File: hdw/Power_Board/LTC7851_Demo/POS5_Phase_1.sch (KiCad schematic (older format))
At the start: 37 parts, among them U301 LTC7851UHH, U401 SiC779

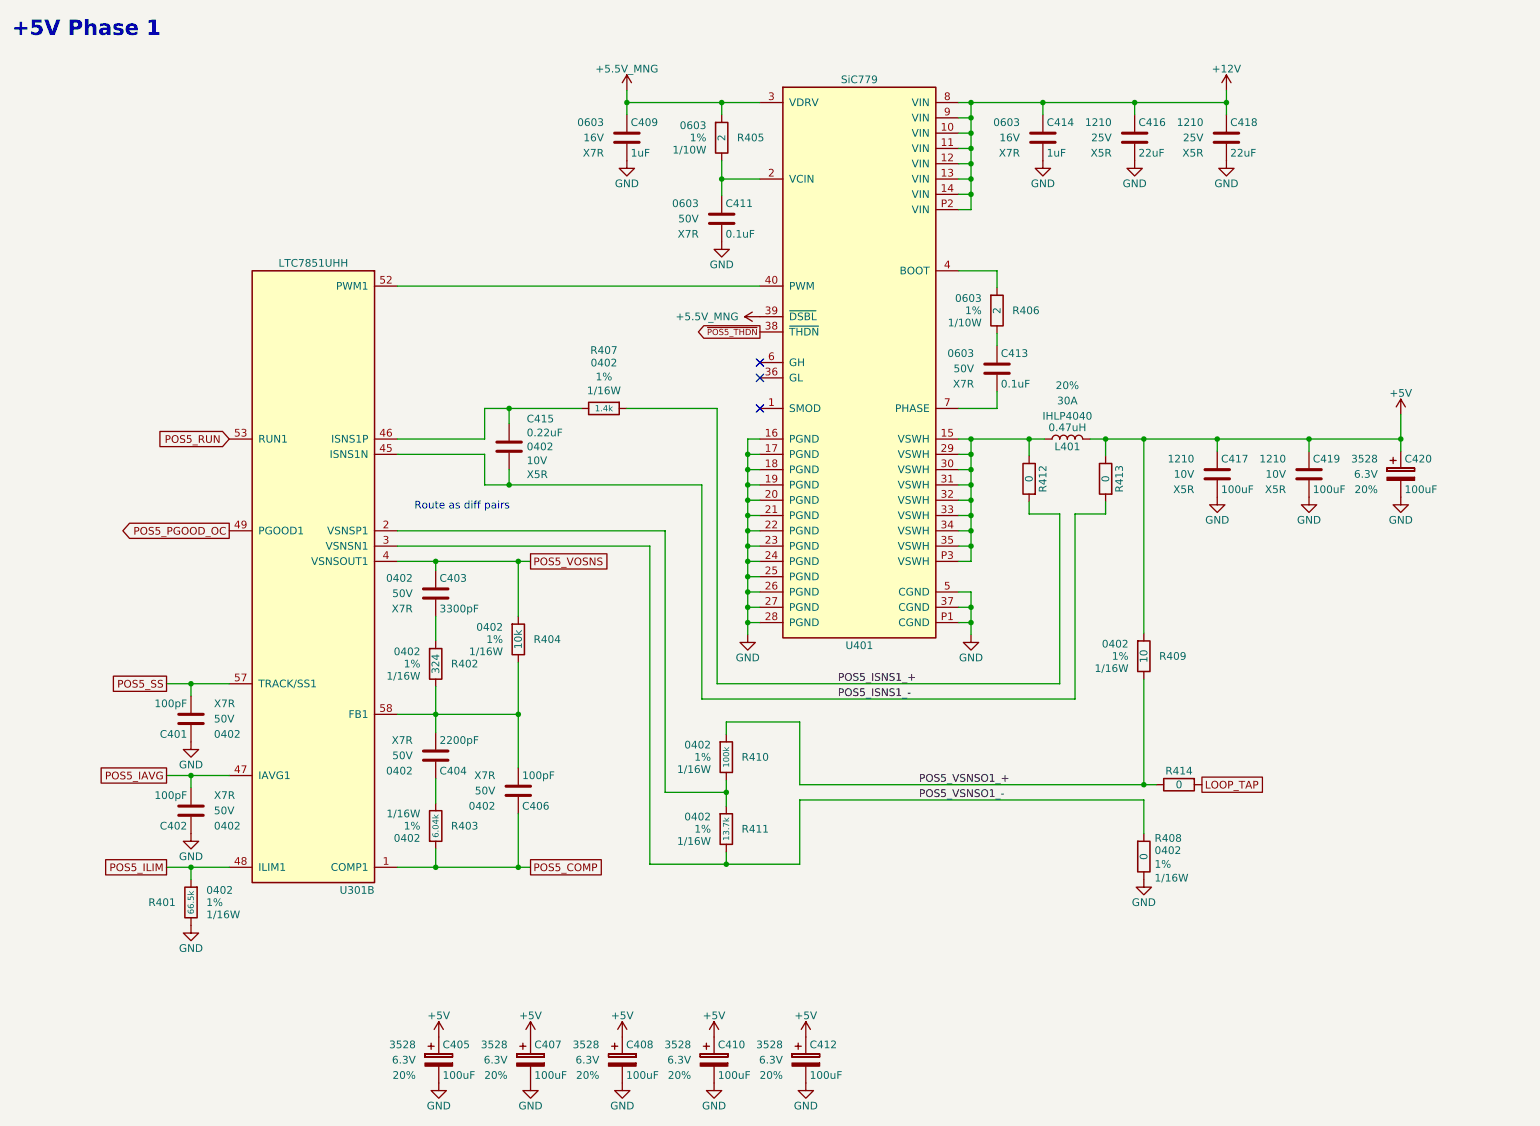
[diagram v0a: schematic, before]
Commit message: Added changes to power board BOM
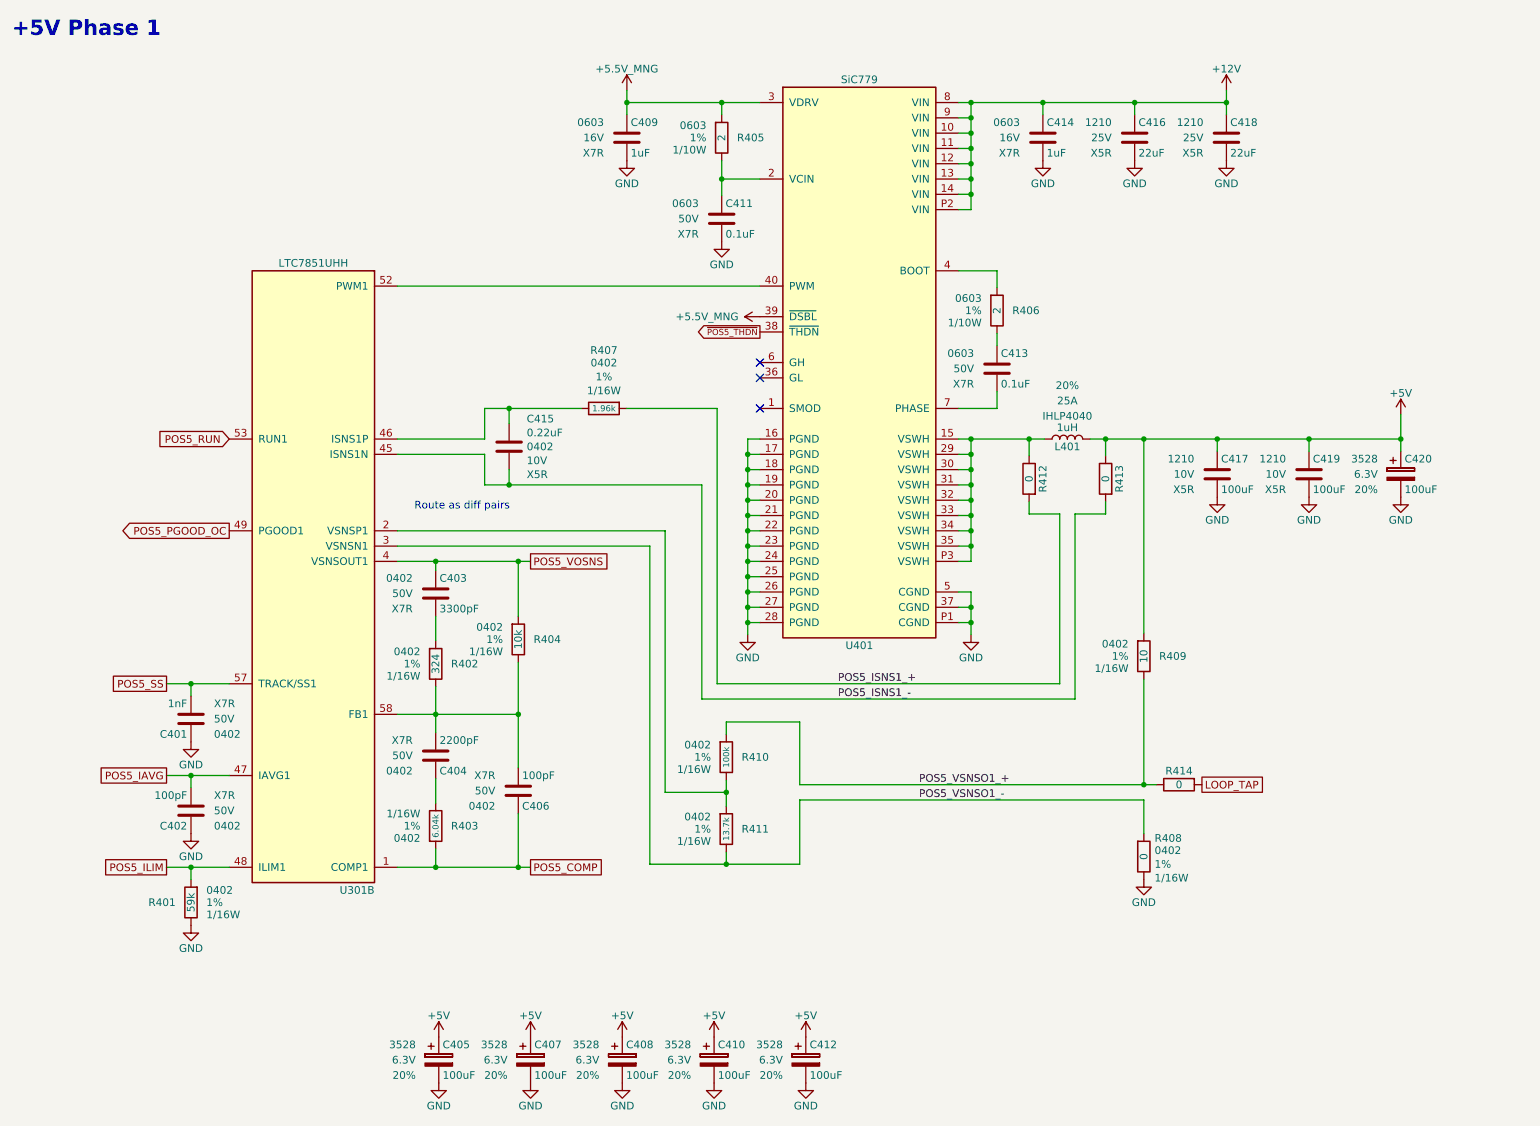
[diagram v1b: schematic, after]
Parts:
- C401: value 100pF -> 1nF; Digi-Key PN 478-1089-1-ND -> 311-1080-1-ND
- L401: value 0.47uH -> 1uH; Ampacity 30A -> 25A; Digi-Key PN 541-2595-1-ND -> 541-1306-1-ND
- R401: value 66.5k -> 59k; Digi-Key PN RMCF0402FT66K5CT-ND -> P59KDCCT-ND
- R407: value 1.4k -> 1.96k; Digi-Key PN RMCF0402FT1K40CT-ND -> 311-1.96KLRCT-ND
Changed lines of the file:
@@
 P 7440 3310
 F 0 "L401" V 7390 3310 50  0000 C CNN
-F 1 "0.47uH" V 7515 3310 50  0000 C CNN
+F 1 "1uH" V 7515 3310 50  0000 C CNN
 F 2 "Inductors_SMD:L_Vishay_IHLP-4040" H 7440 3310 50  0001 C CNN
 F 3 "" H 7440 3310 50  0001 C CNN
-F 4 "541-2595-1-ND" H 7440 3310 50  0001 C CNN "Digi-Key PN"
+F 4 "541-1306-1-ND" H 7440 3310 50  0001 C CNN "Digi-Key PN"
 F 5 "IHLP4040" V 7590 3310 50  0000 C CNN "display_footprint"
-F 6 "30A" V 7690 3310 50  0000 C CNN "Ampacity"
+F 6 "25A" V 7690 3310 50  0000 C CNN "Ampacity"
 F 7 "20%" V 7790 3310 50  0000 C CNN "Tolerance"
 	1    7440 3310
@@
 P 4410 3110
 F 0 "R407" V 4790 3110 50  0000 C CNN
-F 1 "1.4k" V 4410 3110 40  0000 C CNN
+F 1 "1.96k" V 4410 3110 40  0000 C CNN
 F 2 "Resistors_SMD:R_0402" H 4410 3110 50  0001 C CNN
 F 3 "" H 4410 3110 50  0001 C CNN
-F 4 "RMCF0402FT1K40CT-ND" H 4710 3510 60  0001 C CNN "Digi-Key PN"
+F 4 "311-1.96KLRCT-ND" H 4710 3510 60  0001 C CNN "Digi-Key PN"
 F 5 "0402" V 4708 3110 50  0000 C CNN "display_footprint"
 F 6 "1%" V 4617 3110 50  0000 C CNN "Tolerance"
@@
 P 1710 6340
 F 0 "R401" H 1610 6340 50  0000 R CNN
-F 1 "66.5k" V 1710 6340 40  0000 C CNN
+F 1 "59k" V 1710 6340 50  0000 C CNN
 F 2 "Resistors_SMD:R_0402" H 1710 6340 50  0001 C CNN
 F 3 "" H 1710 6340 50  0001 C CNN
-F 4 "RMCF0402FT66K5CT-ND" H 2010 6740 60  0001 C CNN "Digi-Key PN"
+F 4 "P59KDCCT-ND" H 2010 6740 60  0001 C CNN "Digi-Key PN"
 F 5 "0402" H 1810 6420 50  0000 L CNN "display_footprint"
 F 6 "1%" H 1810 6340 50  0000 L CNN "Tolerance"
@@
 P 1710 5140
 F 0 "C401" H 1735 5240 50  0000 L CNN
-F 1 "100pF" H 1735 5040 50  0000 L CNN
+F 1 "1nF" H 1735 5040 50  0000 L CNN
 F 2 "Capacitors_SMD:C_0402" H 1748 4990 50  0001 C CNN
 F 3 "" H 1735 5240 50  0001 C CNN
-F 4 "478-1089-1-ND" H 2135 5640 60  0001 C CNN "Digi-Key PN"
+F 4 "311-1080-1-ND" H 2135 5640 60  0001 C CNN "Digi-Key PN"
 F 5 "0402" H 1560 5240 50  0000 R CNN "display_footprint"
 F 6 "50V" H 1560 5140 50  0000 R CNN "Voltage"

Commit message: Merging drews_branch_3 into master
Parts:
- C401, C402, C403, C404, C406, C409, C411, C413, C414, C415, C416, C417, C418, C419: symbol Custom_Library:C_Custom -> LED_Display_Local_Library:C_Custom
- C405, C407, C408, C410, C412, C420: symbol Custom_Library:CP_Tant_Custom -> LED_Display_Local_Library:CP_Tant_Custom
- L401: symbol Custom_Library:L_Custom -> LED_Display_Local_Library:L_Custom
- R401, R402, R403, R404, R405, R406, R407, R408, R409, R410, R411, R412, R413, R414: symbol Custom_Library:R_Custom -> LED_Display_Local_Library:R_Custom
- U301: symbol Custom_Library:LTC7851UHH -> LED_Display_Local_Library:LTC7851UHH
- U401: symbol Custom_Library:SiC779 -> LED_Display_Local_Library:SiC779
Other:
- note added: "04. +5V Phase 1"
- note removed: "+5V Phase 1"
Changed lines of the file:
@@
 POS5_PGOOD_OC
 $Comp
-L Custom_Library:C_Custom C409
+L LED_Display_Local_Library:C_Custom C409
 U 1 1 5BB875B8
 P 4560 1340
@@
 F 2 "Capacitors_SMD:C_0603" H 4598 1190 50  0001 C CNN
 F 3 "" H 4585 1440 50  0001 C CNN
-F 4 "0603" H 4410 1440 50  0000 R CNN "display_footprint"
-F 5 "16V" H 4410 1340 50  0000 R CNN "Voltage"
-F 6 "X7R" H 4410 1240 50  0000 R CNN "Dielectric"
-F 7 "1276-6524-1-ND" H 4985 1840 60  0001 C CNN "Digi-Key PN"
+F 4 "1276-6524-1-ND" H 4985 1840 60  0001 C CNN "Digi-Key PN"
+F 5 "0603" H 4410 1440 50  0000 R CNN "display_footprint"
+F 6 "16V" H 4410 1340 50  0000 R CNN "Voltage"
+F 7 "X7R" H 4410 1240 50  0000 R CNN "Dielectric"
 	1    4560 1340
 	1    0    0    -1
@@
 $EndComp
 $Comp
-L Custom_Library:SiC779 U401
+L LED_Display_Local_Library:SiC779 U401
 U 1 1 5BB8C7AD
 P 6080 2810
@@
 	6810 3910 6810 4010
 $Comp
-L Custom_Library:L_Custom L401
+L LED_Display_Local_Library:L_Custom L401
 U 1 1 5BB98C10
 P 7440 3310
@@
 	6810 1710 6810 1810
 $Comp
-L Custom_Library:R_Custom R406
+L LED_Display_Local_Library:R_Custom R406
 U 1 1 5BB9AE0E
 P 6980 2470
@@
 $EndComp
 $Comp
-L Custom_Library:C_Custom C413
+L LED_Display_Local_Library:C_Custom C413
 U 1 1 5BB9AE19
 P 6980 2850
@@
 F 2 "Capacitors_SMD:C_0603" H 7018 2700 50  0001 C CNN
 F 3 "" H 7005 2950 50  0001 C CNN
-F 4 "0603" H 6830 2950 50  0000 R CNN "display_footprint"
-F 5 "50V" H 6830 2850 50  0000 R CNN "Voltage"
-F 6 "X7R" H 6830 2750 50  0000 R CNN "Dielectric"
-F 7 "490-4779-1-ND" H 7405 3350 60  0001 C CNN "Digi-Key PN"
+F 4 "490-4779-1-ND" H 7405 3350 60  0001 C CNN "Digi-Key PN"
+F 5 "0603" H 6830 2950 50  0000 R CNN "display_footprint"
+F 6 "50V" H 6830 2850 50  0000 R CNN "Voltage"
+F 7 "X7R" H 6830 2750 50  0000 R CNN "Dielectric"
 	1    6980 2850
 	1    0    0    -1
@@
 	7190 3310 6810 3310
 $Comp
-L Custom_Library:R_Custom R407
+L LED_Display_Local_Library:R_Custom R407
 U 1 1 5BBBB2FC
 P 4410 3110
@@
 $EndComp
 $Comp
-L Custom_Library:C_Custom C415
+L LED_Display_Local_Library:C_Custom C415
 U 1 1 5BBBEAA9
 P 3790 3360
@@
 	3790 3610 3630 3610
 $Comp
-L Custom_Library:C_Custom C416
+L LED_Display_Local_Library:C_Custom C416
 U 1 1 5BBCE509
 P 7880 1340
@@
 	8480 1110 7880 1110
 $Comp
-L Custom_Library:C_Custom C417
+L LED_Display_Local_Library:C_Custom C417
 U 1 1 5BBD7D44
 P 8420 3540
@@
 F 2 "Capacitors_SMD:C_1210" H 8458 3390 50  0001 C CNN
 F 3 "" H 8445 3640 50  0001 C CNN
-F 4 "1210" H 8270 3640 50  0000 R CNN "display_footprint"
-F 5 "10V" H 8270 3540 50  0000 R CNN "Voltage"
-F 6 "X5R" H 8270 3440 50  0000 R CNN "Dielectric"
-F 7 "587-3432-1-ND" H 8845 4040 60  0001 C CNN "Digi-Key PN"
+F 4 "587-3432-1-ND" H 8845 4040 60  0001 C CNN "Digi-Key PN"
+F 5 "1210" H 8270 3640 50  0000 R CNN "display_footprint"
+F 6 "10V" H 8270 3540 50  0000 R CNN "Voltage"
+F 7 "X5R" H 8270 3440 50  0000 R CNN "Dielectric"
 	1    8420 3540
 	1    0    0    -1
@@
 Connection ~ 7940 3310
 $Comp
-L Custom_Library:R_Custom R410
+L LED_Display_Local_Library:R_Custom R410
 U 1 1 5BC4AD64
 P 5210 5390
@@
 $EndComp
 $Comp
-L Custom_Library:C_Custom C404
+L LED_Display_Local_Library:C_Custom C404
 U 1 1 5BC8C461
 P 3310 5380
@@
 	3310 5530 3310 5690
 $Comp
-L Custom_Library:C_Custom C406
+L LED_Display_Local_Library:C_Custom C406
 U 1 1 5BC913E8
 P 3850 5610
@@
 $EndComp
 $Comp
-L Custom_Library:C_Custom C403
+L LED_Display_Local_Library:C_Custom C403
 U 1 1 5BC9167C
 P 3310 4320
@@
 	3310 4470 3310 4630
 $Comp
-L Custom_Library:LTC7851UHH U301
+L LED_Display_Local_Library:LTC7851UHH U301
 U 2 1 5BCC0888
 P 2510 4210
@@
 Connection ~ 3850 6110
 $Comp
-L Custom_Library:R_Custom R401
+L LED_Display_Local_Library:R_Custom R401
 U 1 1 5BDE1E17
 P 1710 6340
@@
 $EndComp
 $Comp
-L Custom_Library:C_Custom C411
+L LED_Display_Local_Library:C_Custom C411
 U 1 1 5BBF5660
 P 5180 1870
@@
 F 2 "Capacitors_SMD:C_0603" H 5218 1720 50  0001 C CNN
 F 3 "" H 5205 1970 50  0001 C CNN
-F 4 "0603" H 5030 1970 50  0000 R CNN "display_footprint"
-F 5 "50V" H 5030 1870 50  0000 R CNN "Voltage"
-F 6 "X7R" H 5030 1770 50  0000 R CNN "Dielectric"
-F 7 "490-4779-1-ND" H 5605 2370 60  0001 C CNN "Digi-Key PN"
+F 4 "490-4779-1-ND" H 5605 2370 60  0001 C CNN "Digi-Key PN"
+F 5 "0603" H 5030 1970 50  0000 R CNN "display_footprint"
+F 6 "50V" H 5030 1870 50  0000 R CNN "Voltage"
+F 7 "X7R" H 5030 1770 50  0000 R CNN "Dielectric"
 	1    5180 1870
 	1    0    0    -1
 $EndComp
 $Comp
-L Custom_Library:R_Custom R405
+L LED_Display_Local_Library:R_Custom R405
 U 1 1 5BBF579B
 P 5180 1340
@@
 	8480 1030 8480 1110
 $Comp
-L Custom_Library:R_Custom R409
+L LED_Display_Local_Library:R_Custom R409
 U 1 1 5BBFEF87
 P 7940 4730
@@
 LOOP_TAP
 $Comp
-L Custom_Library:C_Custom C414
+L LED_Display_Local_Library:C_Custom C414
 U 1 1 5BC2428E
 P 7280 1340
@@
 F 2 "Capacitors_SMD:C_0603" H 7318 1190 50  0001 C CNN
 F 3 "" H 7305 1440 50  0001 C CNN
-F 4 "0603" H 7130 1440 50  0000 R CNN "display_footprint"
-F 5 "16V" H 7130 1340 50  0000 R CNN "Voltage"
-F 6 "X7R" H 7130 1240 50  0000 R CNN "Dielectric"
-F 7 "1276-6524-1-ND" H 7705 1840 60  0001 C CNN "Digi-Key PN"
+F 4 "1276-6524-1-ND" H 7705 1840 60  0001 C CNN "Digi-Key PN"
+F 5 "0603" H 7130 1440 50  0000 R CNN "display_footprint"
+F 6 "16V" H 7130 1340 50  0000 R CNN "Voltage"
+F 7 "X7R" H 7130 1240 50  0000 R CNN "Dielectric"
 	1    7280 1340
 	1    0    0    -1
@@
 Connection ~ 9020 3310
 $Comp
-L Custom_Library:CP_Tant_Custom C420
+L LED_Display_Local_Library:CP_Tant_Custom C420
 U 1 1 5BC70CA8
 P 9620 3540
@@
 $EndComp
 $Comp
-L Custom_Library:C_Custom C419
+L LED_Display_Local_Library:C_Custom C419
 U 1 1 5BC8633B
 P 9020 3540
@@
 $EndComp
 $Comp
-L Custom_Library:C_Custom C418
+L LED_Display_Local_Library:C_Custom C418
 U 1 1 5BC8FEA3
 P 8480 1340
@@
 $EndComp
 $Comp
-L Custom_Library:CP_Tant_Custom C405
+L LED_Display_Local_Library:CP_Tant_Custom C405
 U 1 1 5BC96F62
 P 3330 7370
@@
 $EndComp
 $Comp
-L Custom_Library:CP_Tant_Custom C407
+L LED_Display_Local_Library:CP_Tant_Custom C407
 U 1 1 5BC9711C
 P 3930 7370
@@
 $EndComp
 $Comp
-L Custom_Library:CP_Tant_Custom C408
+L LED_Display_Local_Library:CP_Tant_Custom C408
 U 1 1 5BC9718A
 P 4530 7370
@@
 $EndComp
 $Comp
-L Custom_Library:CP_Tant_Custom C410
+L LED_Display_Local_Library:CP_Tant_Custom C410
 U 1 1 5BC9721B
 P 5130 7370
@@
 $EndComp
 $Comp
-L Custom_Library:CP_Tant_Custom C412
+L LED_Display_Local_Library:CP_Tant_Custom C412
 U 1 1 5BC97297
 P 5730 7370
@@
 $EndComp
 $Comp
-L Custom_Library:R_Custom R411
+L LED_Display_Local_Library:R_Custom R411
 U 1 1 5BC9933B
 P 5210 5860
@@
 $EndComp
 $Comp
-L Custom_Library:R_Custom R404
+L LED_Display_Local_Library:R_Custom R404
 U 1 1 5BCA05EA
 P 3850 4620
@@
 $EndComp
 $Comp
-L Custom_Library:R_Custom R402
+L LED_Display_Local_Library:R_Custom R402
 U 1 1 5BCA086C
 P 3310 4780
@@
 $EndComp
 $Comp
-L Custom_Library:R_Custom R403
+L LED_Display_Local_Library:R_Custom R403
 U 1 1 5BCA08FE
 P 3310 5840
@@
 Connection ~ 3850 5110
 $Comp
-L Custom_Library:R_Custom R408
+L LED_Display_Local_Library:R_Custom R408
 U 1 1 5BD013D0
 P 7940 6040
@@
 Connection ~ 6810 4010
 Text Notes 540  690  0    100  ~ 20
-+5V Phase 1
+04. +5V Phase 1
 NoConn ~ 5430 2810
 NoConn ~ 5430 2910
@@
 $EndComp
 $Comp
-L Custom_Library:C_Custom C401
+L LED_Display_Local_Library:C_Custom C401
 U 1 1 5BD9BA31
 P 1710 5140
@@
 $EndComp
 $Comp
-L Custom_Library:C_Custom C402
+L LED_Display_Local_Library:C_Custom C402
 U 1 1 5BDA2680
 P 1710 5740
@@
 	3630 3410 3060 3410
 $Comp
-L Custom_Library:R_Custom R412
+L LED_Display_Local_Library:R_Custom R412
 U 1 1 5BDBC574
 P 7190 3570
@@
 $EndComp
 $Comp
-L Custom_Library:R_Custom R413
+L LED_Display_Local_Library:R_Custom R413
 U 1 1 5BDC36EE
 P 7690 3570
@@
 POS5_VSNSO1_+
 $Comp
-L Custom_Library:R_Custom R414
+L LED_Display_Local_Library:R_Custom R414
 U 1 1 5BF4C2D8
 P 8170 5570
@@
 	0    1    -1   0
 $EndComp
+$Comp
+L LED_Display_Local_Library:MU_Logo #G?
+U 1 1 5C003BFF
+P 9900 1100
+F 0 "#G?" H 9900 614 60  0001 C CNN
+F 1 "MU_Logo" H 9900 1586 60  0001 C CNN
+F 2 "" H 9900 1100 50  0001 C CNN
+F 3 "" H 9900 1100 50  0001 C CNN
+	1    9900 1100
+	1    0    0    -1
+$EndComp
 $EndSCHEMATC

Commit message: Schematic cleanup
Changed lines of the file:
@@
 Date "2018-11-28"
 Rev "A"
-Comp "Marquette Senior Design 2018, Group E44"
+Comp "Marquette University Senior Design 2018 Group E44"
 Comment1 ""
 Comment2 ""
@@
 U 1 1 5BC4AD64
 P 5210 5390
-F 0 "R410" H 5110 5390 50  0000 R CNN
+F 0 "R410" H 5150 5390 50  0000 R CNN
 F 1 "100k" V 5210 5390 40  0000 C CNN
 F 2 "Resistors_SMD:R_0402" H 5210 5390 50  0001 C CNN
@@
 U 1 1 5BDE1E17
 P 1710 6340
-F 0 "R401" H 1610 6340 50  0000 R CNN
+F 0 "R401" H 1650 6340 50  0000 R CNN
 F 1 "59k" V 1710 6340 50  0000 C CNN
 F 2 "Resistors_SMD:R_0402" H 1710 6340 50  0001 C CNN
@@
 U 1 1 5BBF579B
 P 5180 1340
-F 0 "R405" H 5080 1340 50  0000 R CNN
+F 0 "R405" H 5120 1340 50  0000 R CNN
 F 1 "2" V 5180 1340 50  0000 C CNN
 F 2 "Resistors_SMD:R_0603" H 5180 1340 50  0001 C CNN
@@
 U 1 1 5BBFEF87
 P 7940 4730
-F 0 "R409" H 7840 4730 50  0000 R CNN
+F 0 "R409" H 7880 4730 50  0000 R CNN
 F 1 "10" V 7940 4730 50  0000 C CNN
 F 2 "Resistors_SMD:R_0402" H 7940 4730 50  0001 C CNN
@@
 U 1 1 5BC9933B
 P 5210 5860
-F 0 "R411" H 5110 5860 50  0000 R CNN
+F 0 "R411" H 5150 5860 50  0000 R CNN
 F 1 "13.7k" V 5210 5860 40  0000 C CNN
 F 2 "Resistors_SMD:R_0402" H 5210 5860 50  0001 C CNN
@@
 U 1 1 5BCA05EA
 P 3850 4620
-F 0 "R404" H 3750 4620 50  0000 R CNN
+F 0 "R404" H 3790 4620 50  0000 R CNN
 F 1 "10k" V 3850 4620 50  0000 C CNN
 F 2 "Resistors_SMD:R_0402" H 3850 4620 50  0001 C CNN
@@
 U 1 1 5BCA086C
 P 3310 4780
-F 0 "R402" H 3210 4780 50  0000 R CNN
+F 0 "R402" H 3250 4780 50  0000 R CNN
 F 1 "324" V 3310 4780 50  0000 C CNN
 F 2 "Resistors_SMD:R_0402" H 3310 4780 50  0001 C CNN
@@
 U 1 1 5BCA08FE
 P 3310 5840
-F 0 "R403" H 3210 5840 50  0000 R CNN
+F 0 "R403" H 3250 5840 50  0000 R CNN
 F 1 "6.04k" V 3310 5840 40  0000 C CNN
 F 2 "Resistors_SMD:R_0402" H 3310 5840 50  0001 C CNN
@@
 U 1 1 5BD013D0
 P 7940 6040
-F 0 "R408" H 7870 6160 50  0000 R CNN
+F 0 "R408" H 8000 6040 50  0000 L CNN
 F 1 "0" V 7940 6040 50  0000 C CNN
 F 2 "Resistors_SMD:R_0402" H 7940 6040 50  0001 C CNN
@@
 U 1 1 5BDBC574
 P 7190 3570
-F 0 "R412" V 7280 3570 50  0000 C CNN
+F 0 "R412" H 7240 3570 50  0000 L CNN
 F 1 "0" V 7190 3570 50  0000 C CNN
 F 2 "Resistors_SMD:R_0402" H 7190 3570 50  0001 C CNN
@@
 U 1 1 5BDC36EE
 P 7690 3570
-F 0 "R413" V 7780 3570 50  0000 C CNN
+F 0 "R413" H 7740 3570 50  0000 L CNN
 F 1 "0" V 7690 3570 50  0000 C CNN
 F 2 "Resistors_SMD:R_0402" H 7690 3570 50  0001 C CNN
@@
 F 3 "" H 8170 5570 50  0001 C CNN
 F 4 "RMCF0402ZT0R00CT-ND" H 8470 5970 60  0001 C CNN "Digi-Key PN"
-F 5 "0402" V 7873 5570 50  0001 C CNN "display_footprint"
-F 6 "1%" V 7964 5570 50  0001 C CNN "Tolerance"
-F 7 "1/16W" V 8055 5570 50  0001 C CNN "Wattage"
+F 5 "0402" V 7873 5570 50  0000 C CNN "display_footprint"
+F 6 "1%" V 7964 5570 50  0000 C CNN "Tolerance"
+F 7 "1/16W" V 8055 5570 50  0000 C CNN "Wattage"
 	1    8170 5570
-	0    1    -1   0
-$EndComp
-$Comp
+	0    1    1    0
+$EndComp
+$Comp
